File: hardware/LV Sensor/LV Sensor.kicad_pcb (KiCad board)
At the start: 2 copper layers, 75 parts, among them J1 Conn_01x04_Pin, J2 Conn_01x02_Pin, J3 TH, J4 TH, J5 TH, J6 TH, SW1 SW_Push, U1 MSPM0G3507 RHB32, U10 DXTN80100CFGQ, U2 ISO1042BDW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

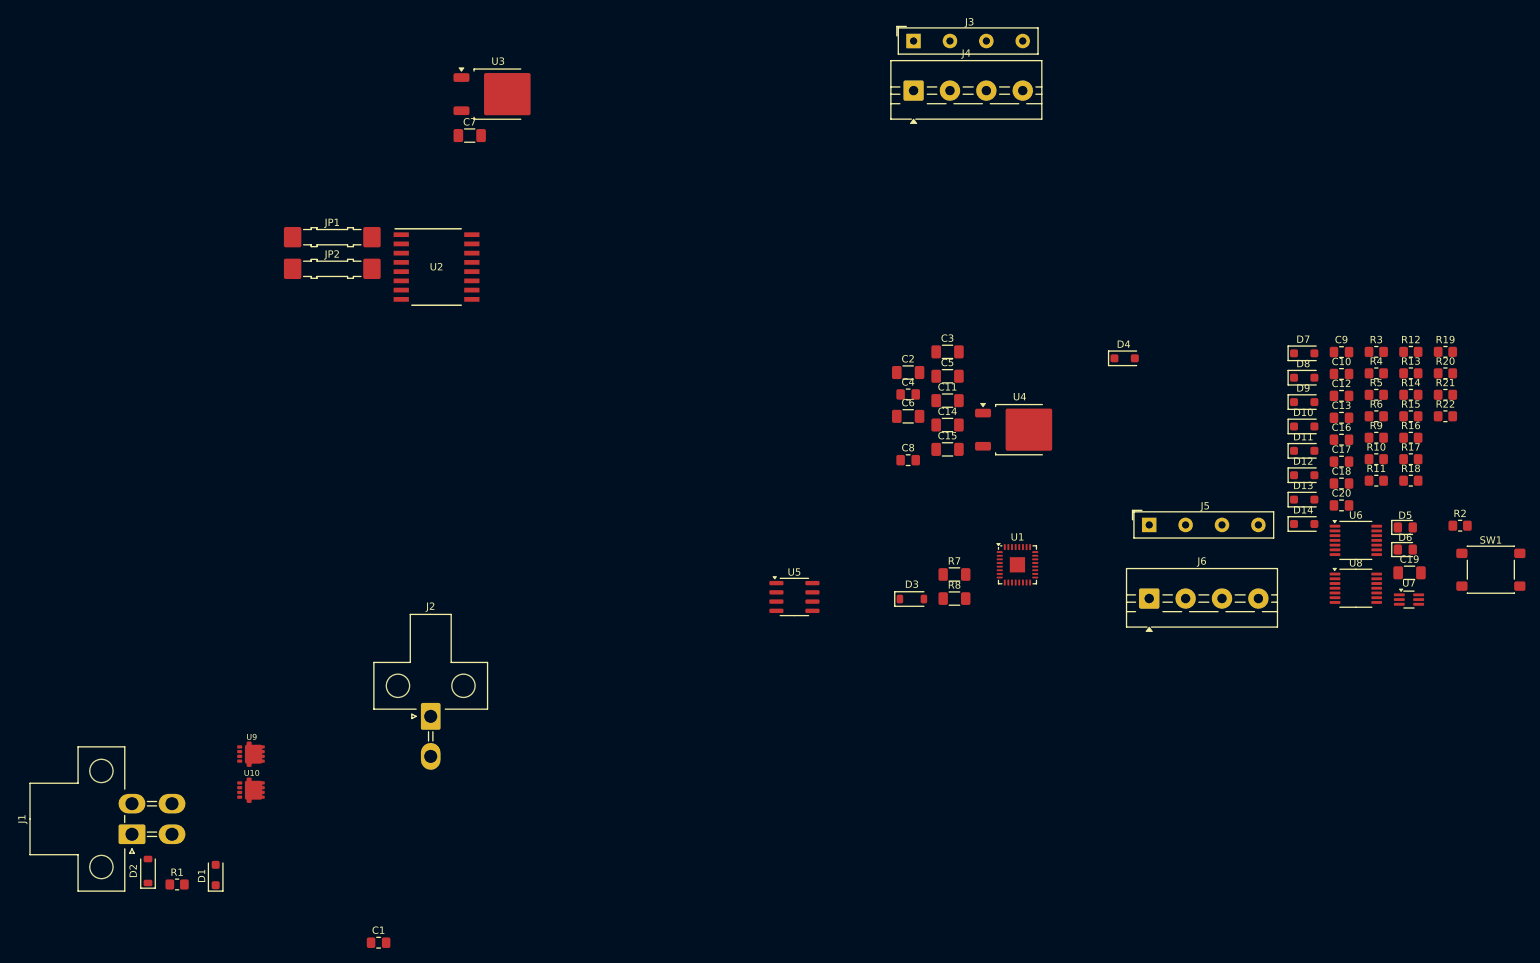
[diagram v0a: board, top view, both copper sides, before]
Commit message: noteed TODOs on LV sensor board
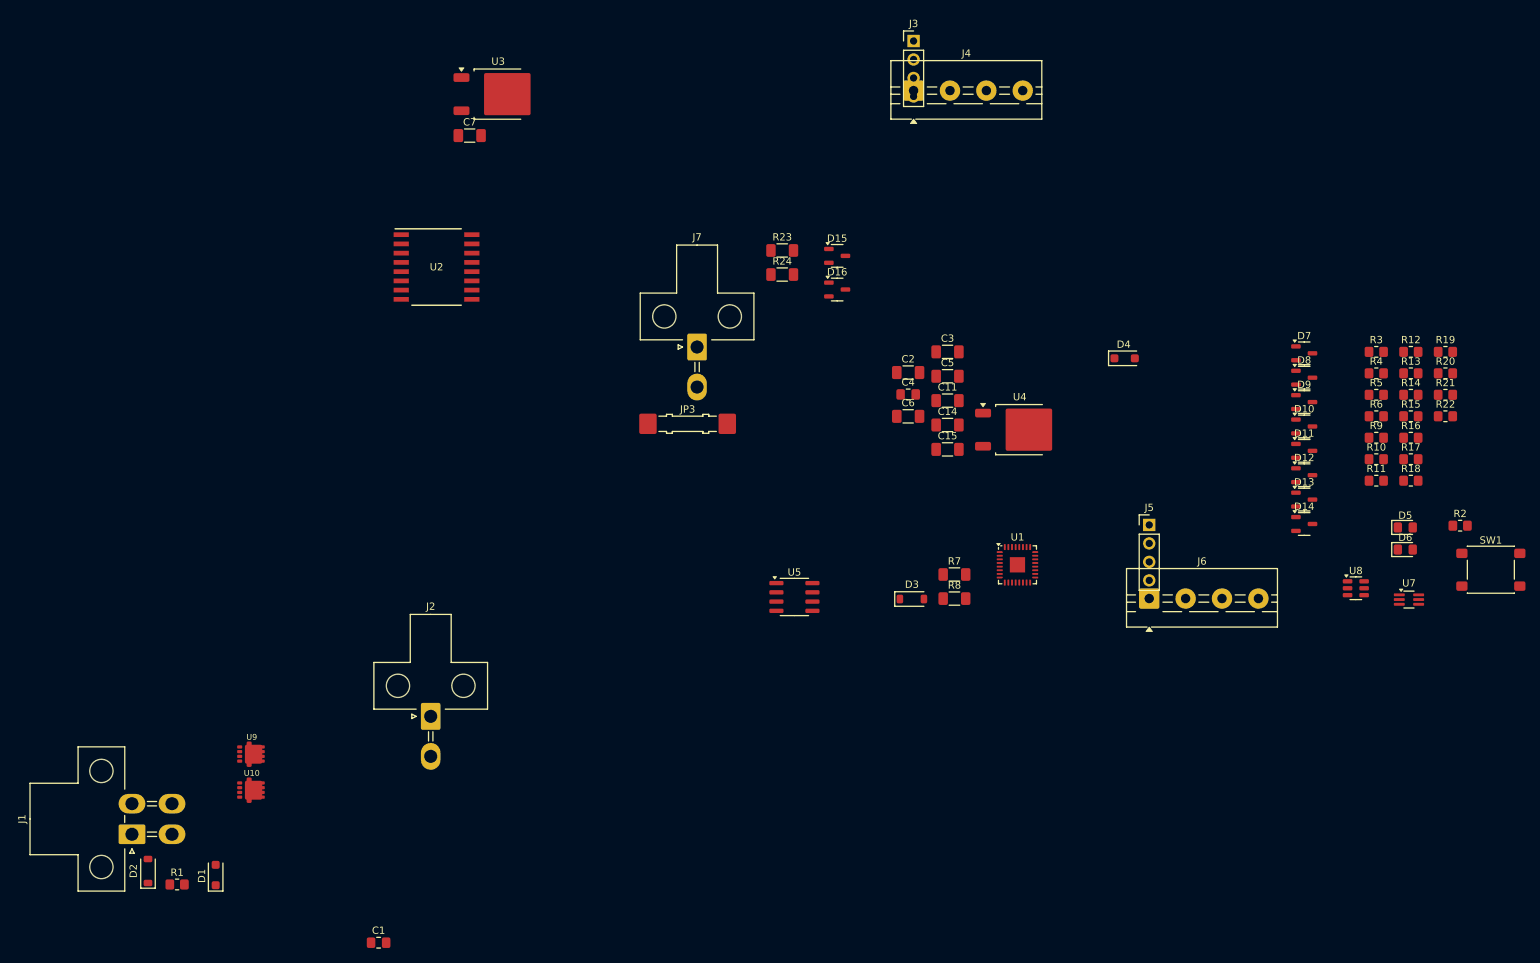
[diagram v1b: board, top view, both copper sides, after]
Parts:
- removed C10, C12, C13, C16, C17, C18, C20, C8, C9: 470n, Capacitor_SMD:C_0805_2012Metric_Pad1.18x1.45mm_HandSolder
- removed C19: 10u, Capacitor_SMD:C_1206_3216Metric_Pad1.33x1.80mm_HandSolder
- removed JP1, JP2: Jumper_2_Open, Jumper:Jumper_Harwin_S1621_P10.9mm
- removed U6: LM324BAIPWR, Package_SO:TSSOP-14_4.4x5mm_P0.65mm
- added D15: BAT54S, Package_TO_SOT_SMD:SOT-23-3, F.Cu at (133.2, 77.6)
- added D16: BAT54S, Package_TO_SOT_SMD:SOT-23-3, F.Cu at (133.2, 82.2)
- added J7: Conn_01x02_Pin, Connector_Molex:Molex_Mini-Fit_Jr_5569-02A1_2x01_P4.20mm_Horizontal, F.Cu at (114.0, 90.2)
- added JP3: Jumper_2_Open, Jumper:Jumper_Harwin_S1621_P10.9mm, F.Cu at (112.7, 100.7)
- added R23: 4.99k, Resistor_SMD:R_1206_3216Metric_Pad1.30x1.75mm_HandSolder, F.Cu at (125.7, 76.9)
- added R24: 4.99k, Resistor_SMD:R_1206_3216Metric_Pad1.30x1.75mm_HandSolder, F.Cu at (125.7, 80.2)
- D10, D11, D12, D13, D14, D7, D8, D9: value 3V -> BAT54S; footprint Diode_SMD:D_SOD-123F -> Package_TO_SOT_SMD:SOT-23-3
- J3, J5: footprint Diode_THT:Diode_Bridge_19.0x3.5x10.0mm_P5.0mm -> Connector_PinHeader_2.54mm:PinHeader_1x04_P2.54mm_Vertical
- J4, J6: value TH -> SCREW
- R10, R11, R15, R16, R18, R19, R5, R9: value 316k -> 100k
- R12, R13, R14, R17, R20, R21, R22, R6: value 54.9k -> 100k
- U8: value LM324BAIPWR -> MCP3421A0T-ECH; footprint Package_SO:TSSOP-14_4.4x5mm_P0.65mm -> Package_TO_SOT_SMD:SOT-23-6
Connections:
- net /LV+ renamed +BATT
- C11 pad 2: GND -> -BATT
- C14 pad 1: +3.3V -> +3V3
- C14 pad 2: GND -> -BATT
- C15 pad 1: +3.3V -> +3V3
- C15 pad 2: GND -> -BATT
- C2 pad 2: GND -> -BATT
- C3 pad 2: GND -> -BATT
- C4 pad 2: GND -> -BATT
- C5 pad 2: GND -> -BATT
- C6 pad 1: +5V -> Net-(J7-Pin_2)
- C6 pad 2: GND -> -BATT
- D10 pad 1: Net-(D10-K) -> -BATT
- D10 pad 2: GND -> +3V3
- D11 pad 1: Net-(D11-K) -> -BATT
- D11 pad 2: GND -> +3V3
- D12 pad 1: Net-(D12-K) -> -BATT
- D12 pad 2: GND -> +3V3
- D13 pad 1: Net-(D13-K) -> -BATT
- D13 pad 2: GND -> +3V3
- D14 pad 1: Net-(D14-K) -> -BATT
- D14 pad 2: GND -> +3V3
- D4 pad 2: GND -> -BATT
- D5 pad 1: GND -> -BATT
- D6 pad 1: GND -> -BATT
- D7 pad 1: Net-(D14-K) -> -BATT
- D7 pad 2: GND -> +3V3
- D8 pad 1: Net-(D11-K) -> -BATT
- D8 pad 2: GND -> +3V3
- D9 pad 1: Net-(D9-K) -> -BATT
- D9 pad 2: GND -> +3V3
- J2 pad 2: GND -> -BATT
- R10 pad 1: Net-(J3-Pin_2) -> Net-(J3-Pin_4)
- R10 pad 2: Net-(D10-K) -> /ADC0_3
- R11 pad 1: Net-(J3-Pin_1) -> -BATT
- R11 pad 2: Net-(D9-K) -> /ADC0_0
- R12 pad 1: GND -> -BATT
- R12 pad 2: Net-(D9-K) -> /ADC0_1
- R13 pad 1: GND -> -BATT
- R13 pad 2: Net-(D10-K) -> /ADC0_2
- R14 pad 1: GND -> -BATT
- R14 pad 2: Net-(D11-K) -> /ADC0_3
- R15 pad 1: Net-(J5-Pin_4) -> Net-(J5-Pin_1)
- R15 pad 2: Net-(D14-K) -> /ADC1_0
- R16 pad 1: Net-(J5-Pin_3) -> -BATT
- R16 pad 2: Net-(U8-3IN+) -> /ADC1_0
- R17 pad 1: GND -> Net-(J5-Pin_2)
- R17 pad 2: Net-(D14-K) -> /ADC1_1
- R18 pad 1: Net-(J5-Pin_2) -> -BATT
- R18 pad 2: Net-(D13-K) -> /ADC1_1
- R19 pad 1: Net-(J5-Pin_1) -> Net-(J5-Pin_3)
- R19 pad 2: Net-(D12-K) -> /ADC1_2
- R20 pad 1: GND -> -BATT
- R20 pad 2: Net-(D12-K) -> /ADC1_2
- R21 pad 1: GND -> Net-(J5-Pin_4)
- R21 pad 2: Net-(D13-K) -> /ADC1_3
- R22 pad 1: GND -> -BATT
- R22 pad 2: Net-(D14-K) -> /ADC1_3
- R3 pad 2: +3.3V -> +3V3
- R4 pad 2: +3.3V -> +3V3
- R5 pad 1: Net-(J3-Pin_4) -> Net-(J3-Pin_1)
- R5 pad 2: Net-(D11-K) -> /ADC0_0
- R6 pad 1: GND -> Net-(J3-Pin_2)
- R6 pad 2: Net-(D11-K) -> /ADC0_1
- R7 pad 1: +3.3V -> +3V3
- R8 pad 1: GND -> -BATT
- R9 pad 2: Net-(U6-3IN+) -> /ADC0_2
- SW1 pad 2: GND -> -BATT
- U1 pad 10: unconnected-(U1-PA6_HFXOUT-Pad10) -> /TIMG0_C1
- U1 pad 26: /LED_RED_N -> unconnected-(U1-PA22_A0_7-Pad26)
- U1 pad 27: /LED_GREEN -> unconnected-(U1-PA23_VREF+-Pad27)
- U1 pad 33: GND -> -BATT
- U1 pad 4: +3.3V -> +3V3
- U1 pad 5: GND -> -BATT
- U1 pad 7: /TIMG7_C0 -> /I2C1_SDA
- U1 pad 8: /TIMG7_C1 -> /I2C1_SCL
- U1 pad 9: unconnected-(U1-PA5_HFXIN-Pad9) -> /TIMG0_C0
- U10 pad 2: LINE -> Net-(U10-E)
- U2 pad 2: GND -> -BATT
- U2 pad 8: GND -> -BATT
- U4 pad 1: LINE -> Net-(U10-E)
- U4 pad 2: GND -> -BATT
- U4 pad 3: +5V -> Net-(J7-Pin_2)
- U5 pad 2: GND -> -BATT
- U5 pad 3: GND -> -BATT
- U5 pad 6: GND -> -BATT
- U5 pad 7: GND -> -BATT
- U5 pad 8: +5V -> Net-(U10-E)
- U8 pad 1: /ADC1_0 -> unconnected-(U8-Vin+-Pad1)
- U8 pad 2: /ADC1_0 -> -3V3
- U8 pad 3: Net-(D12-K) -> /I2C1_SCL
- U8 pad 4: LINE -> /I2C1_SDA
- U8 pad 5: Net-(D13-K) -> +3V3
- U8 pad 6: /ADC1_1 -> unconnected-(U8-Vin--Pad6)
